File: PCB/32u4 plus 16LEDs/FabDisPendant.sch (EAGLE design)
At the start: 68 parts, among them IC1 MPR121, U3 ATMEGA32U4, Y1 16MHz

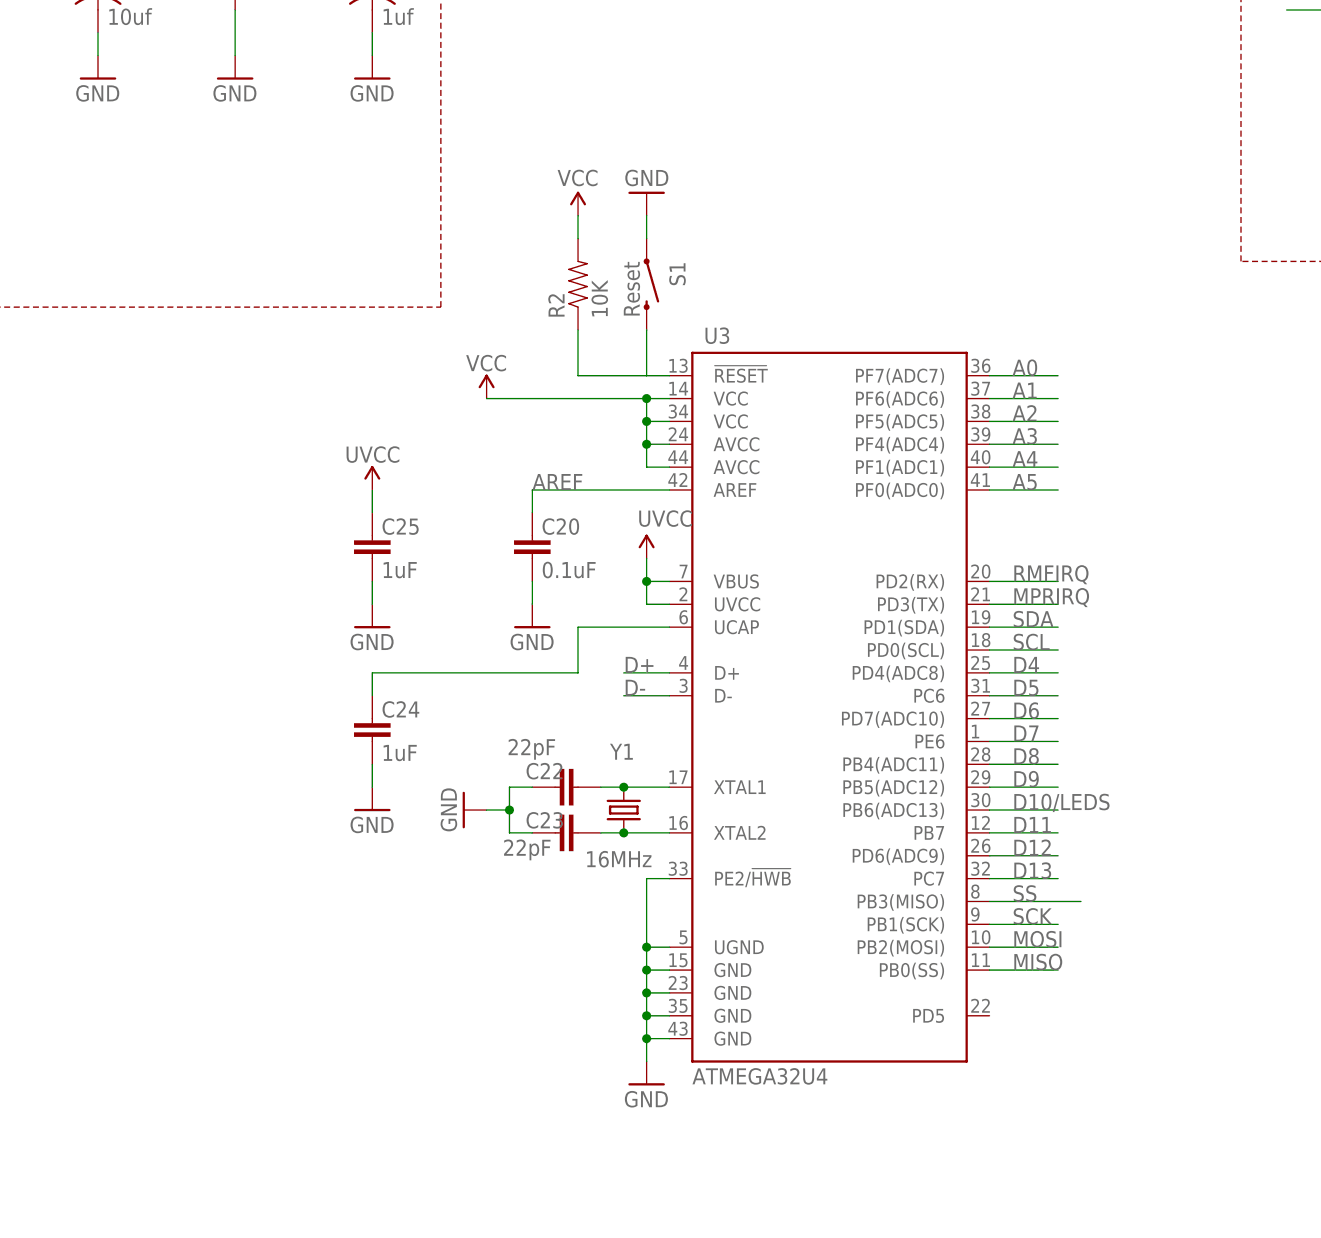
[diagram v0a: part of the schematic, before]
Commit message: Switched from the TQDN package to an AU package
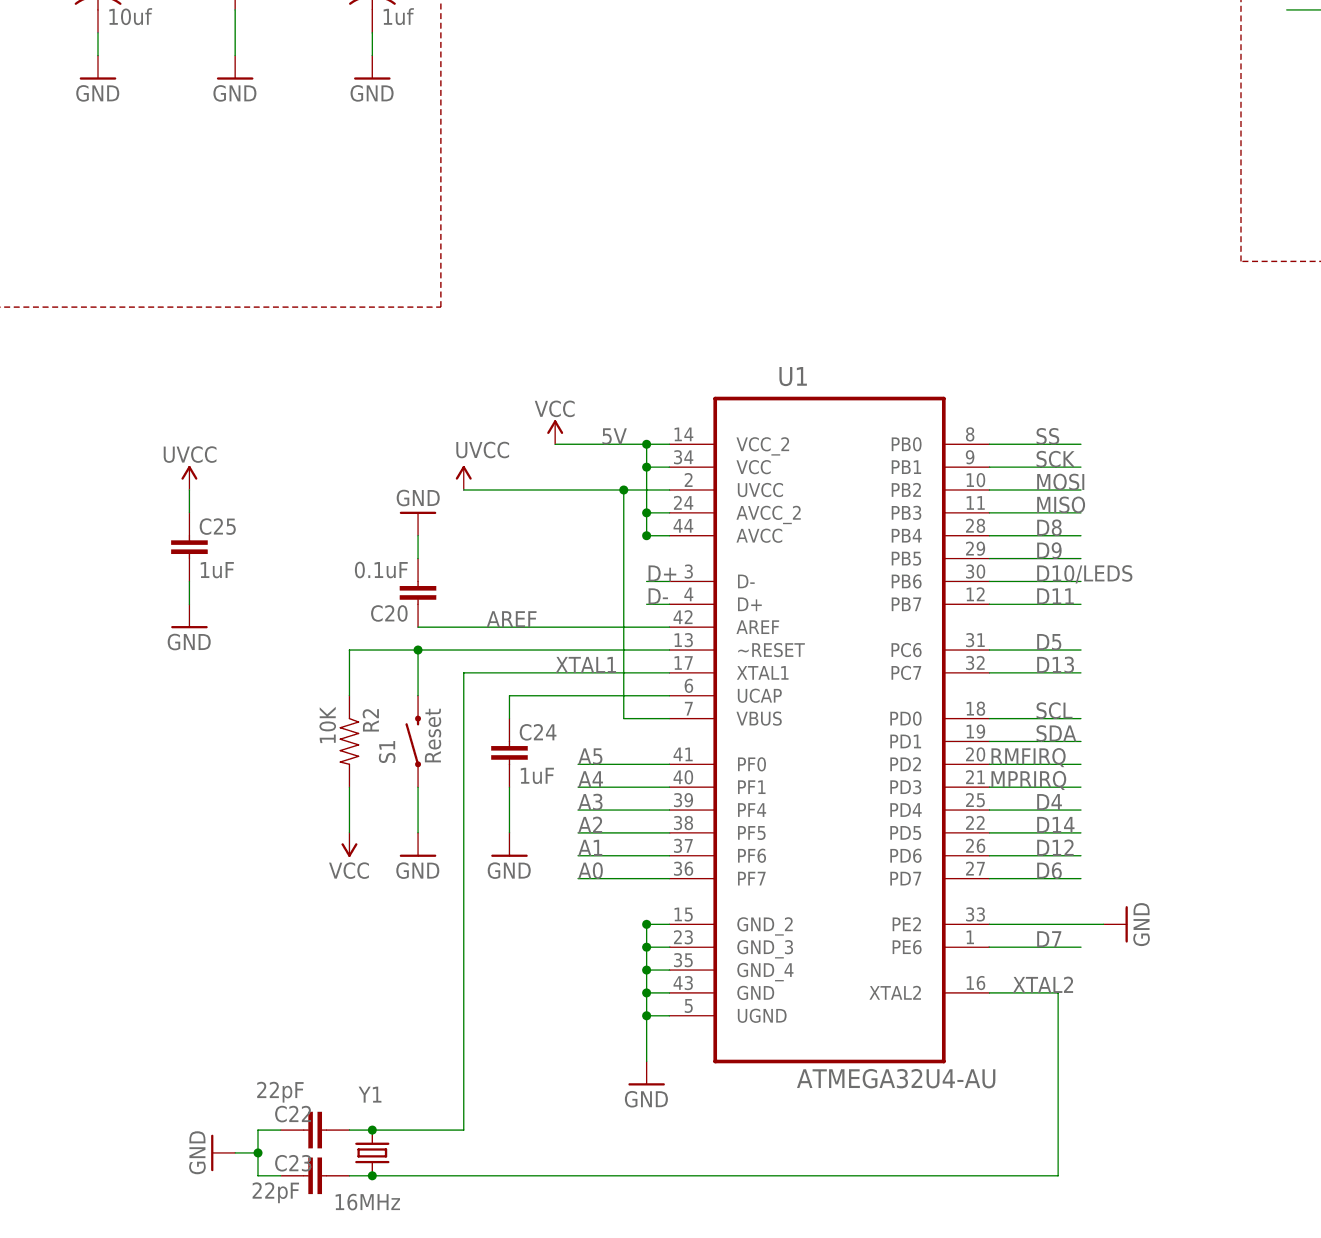
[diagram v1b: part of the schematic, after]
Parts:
- removed U3: ATMEGA32U4, Testing:ATMEGA32U4OUTFAKES
- added U1: ATMEGA32U4-AU, Atmel_By_element14_Batch_1-00:ATMEGA32U4-AU
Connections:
- removed net N$17: C23.1, U3.XTAL2, Y1.1
- removed net N$18: C22.1, U3.XTAL1, Y1.2
- removed net N$19: C24.2, U3.UCAP
- new net D14: U1.PD5
- new net N$55: C24.2, U1.UCAP
- new net XTAL1: C22.1, U1.XTAL1, Y1.2
- new net XTAL2: C23.1, U1.XTAL2, Y1.1
- net 5V: now also U1.AVCC, U1.AVCC_2, U1.VCC, U1.VCC_2; no longer U3.AVCC@24, U3.AVCC@44, U3.VCC@14, U3.VCC@34
- net A0: now also U1.PF7; no longer U3.PF7(ADC7)
- net A1: now also U1.PF6; no longer U3.PF6(ADC6)
- net A2: now also U1.PF5; no longer U3.PF5(ADC5)
- net A3: now also U1.PF4; no longer U3.PF4(ADC4)
- net A4: now also U1.PF1; no longer U3.PF1(ADC1)
- net A5: now also U1.PF0; no longer U3.PF0(ADC0)
- net AREF: now also U1.AREF; no longer U3.AREF
- net D+: now also U1.D-; no longer U3.D+
- net D-: now also U1.D+; no longer U3.D-
- net D10/LEDS: now also U1.PB6; no longer U3.PB6(ADC13)
- net D11: now also U1.PB7; no longer U3.PB7
- net D12: now also U1.PD6; no longer U3.PD6(ADC9)
- net D13: now also U1.PC7; no longer U3.PC7
- net D4: now also U1.PD4; no longer U3.PD4(ADC8)
- net D5: now also U1.PC6; no longer U3.PC6
- net D6: now also U1.PD7; no longer U3.PD7(ADC10)
- net D7: now also U1.PE6; no longer U3.PE6
- net D8: now also U1.PB4; no longer U3.PB4(ADC11)
- net D9: now also U1.PB5; no longer U3.PB5(ADC12)
- net GND: now also U1.GND, U1.GND_2, U1.GND_3, U1.GND_4, U1.PE2, U1.UGND; no longer U3.GND@15, U3.GND@23, U3.GND@35, U3.GND@43, U3.PE2/!HWB, U3.UGND
- net MISO: now also U1.PB3; no longer U3.PB0(SS)
- net MOSI: now also U1.PB2; no longer U3.PB2(MOSI)
- net MPRIRQ: now also U1.PD3; no longer U3.PD3(TX)
- net RESET: now also U1.~RESET; no longer U3.!RESET
- net RMFIRQ: now also U1.PD2; no longer U3.PD2(RX)
- net SCK: now also U1.PB1; no longer U3.PB1(SCK)
- net SCL: now also U1.PD0; no longer U3.PD0(SCL)
- net SDA: now also U1.PD1; no longer U3.PD1(SDA)
- net SS: now also U1.PB0; no longer U3.PB3(MISO)
- net USBVCC: now also U1.UVCC, U1.VBUS; no longer U3.UVCC, U3.VBUS
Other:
- moved on the sheet: C20, C22, C23, C24, C25, R2, S1, Y1
